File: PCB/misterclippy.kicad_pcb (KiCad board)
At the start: 2 copper layers, 30.2 x 109.2 mm, 73 parts, among them J1 PWR, J2 Output Gate, J3 Output Gate, J4 Input, J5 Input, J6 Audio In, J7 Through, J8 Audio In, J9 Through, Q1 BC547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

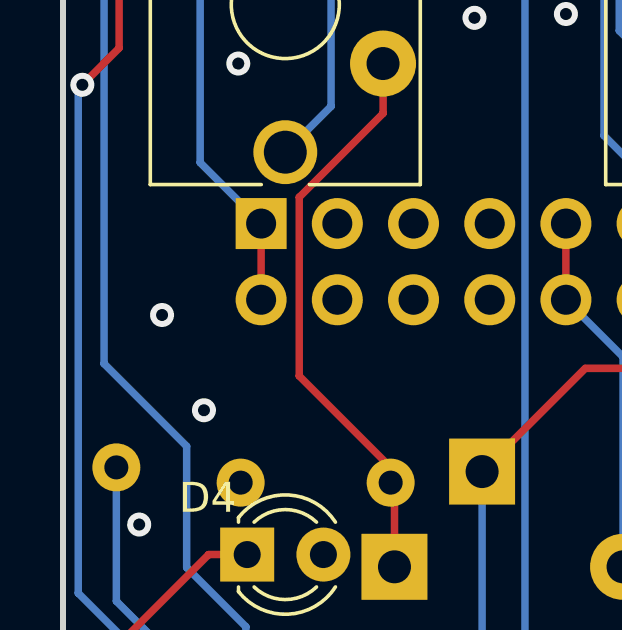
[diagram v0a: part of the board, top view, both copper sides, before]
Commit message: :memo: Add "Red Stripe" marker on the board
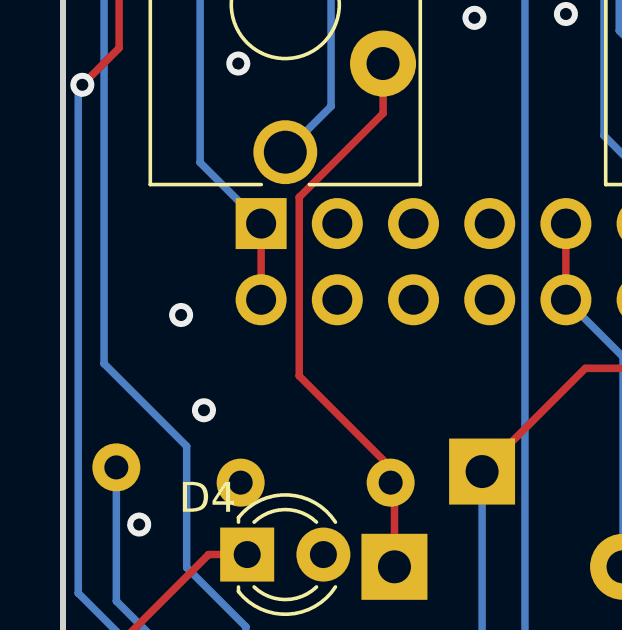
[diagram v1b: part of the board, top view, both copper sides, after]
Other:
- board text added: "Red Stripe (-12V)"
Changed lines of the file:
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@@
     )
   )
+  (gr_line (start 107.315 126.0475) (end 107.315 117.7925)
+    (stroke (width 0.5) (type default)) (layer "B.SilkS"))
   (gr_line locked (start 134.874 160.147) (end 134.874 50.927)
     (stroke (width 0.2) (type solid)) (layer "Edge.Cuts"))
@@
   (gr_text "CC-BY-SA 4.0\nPatrick Pickel\nStefan Haun" (at 125.984 117.221) (layer "B.SilkS")
     (effects (font (size 0.6 0.6) (thickness 0.1) bold) (justify bottom mirror))
+  )
+  (gr_text "Red Stripe (-12V)" (at 106.045 126.0475 270) (layer "B.SilkS")
+    (effects (font (size 0.6 0.6) (thickness 0.1) bold) (justify left bottom mirror))
   )
   (segment (start 129.032 98.806) (end 128.726 99.112) (width 0.25) (layer "F.Cu") (net 1))
@@
   (via (at 114.3 56.134) (size 0.8) (drill 0.4) (layers "F.Cu" "B.Cu") (free) (net 2))
   (via (at 115.062 108.204) (size 0.8) (drill 0.4) (layers "F.Cu" "B.Cu") (free) (net 2))
-  (via (at 107.95 124.968) (size 0.8) (drill 0.4) (layers "F.Cu" "B.Cu") (free) (net 2))
+  (via (at 108.585 124.968) (size 0.8) (drill 0.4) (layers "F.Cu" "B.Cu") (free) (net 2))
   (via (at 118.618 154.686) (size 0.8) (drill 0.4) (layers "F.Cu" "B.Cu") (free) (net 2))
   (via (at 129.2435 74.168) (size 0.8) (drill 0.4) (layers "F.Cu" "B.Cu") (net 2))
